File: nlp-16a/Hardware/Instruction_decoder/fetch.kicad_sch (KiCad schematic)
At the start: 50 parts

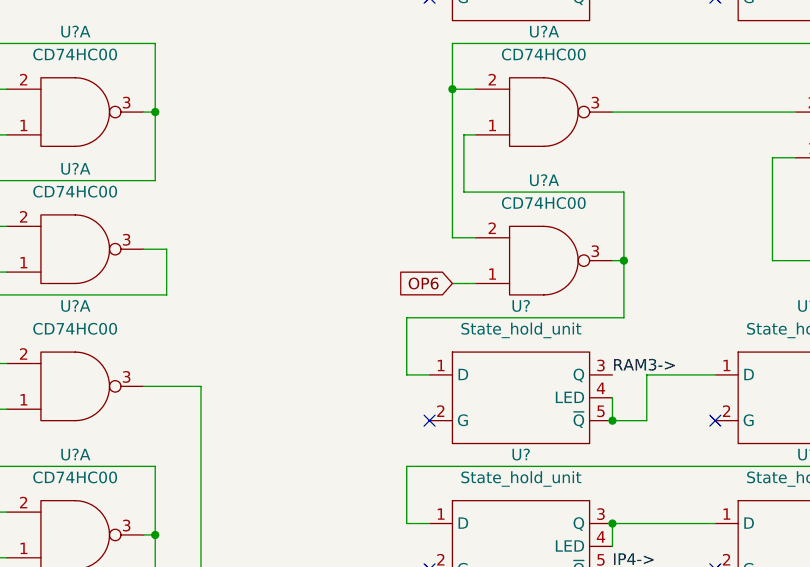
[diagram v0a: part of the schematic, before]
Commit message: 命令デコーダ 不具合修正
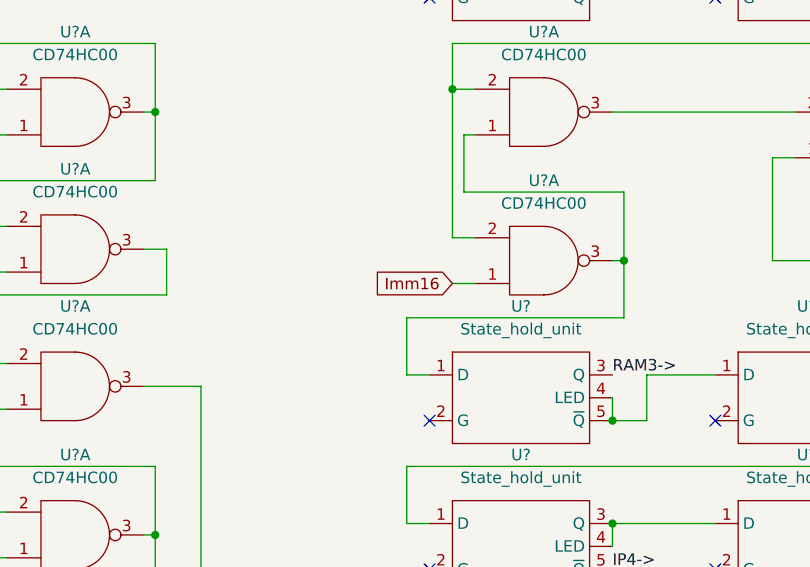
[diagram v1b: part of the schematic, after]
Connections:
- net OP6: no longer U?.1
- new net Imm16: U?.1
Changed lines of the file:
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@@
     )
   )
-  (global_label "OP6" (shape input) (at 147.32 88.9 180) (fields_autoplaced)
+  (global_label "Imm16" (shape input) (at 147.32 88.9 180) (fields_autoplaced)
     (effects (font (size 1.27 1.27)) (justify right))
-    (property "Intersheet References" "${INTERSHEET_REFS}" (id 0) (at 141.0969 88.8206 0)
+    (property "Intersheet References" "${INTERSHEET_REFS}" (id 0) (at 138.4964 88.8206 0)
       (effects (font (size 1.27 1.27)) (justify right) hide)
     )

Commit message: 命令デコーダ ロジック部の設計だいたい完了git statusgit statusやったぜ
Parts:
- removed U? (x14): CD74HC00, Package_DIP:DIP-14_W7.62mm, symbol CD74HCXX:CD74HC00
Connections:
- net ->Address1 renamed ~{->IP_SET}
- net ->Address2 renamed ~{->IP_INC1}
- net ->Address3 renamed ~{->IP_INC2}
- net ->Address4 renamed ~{->IP_INC3}
- net IP1-> renamed ~{IP_SET->}
- net IP2-> renamed ~{IP_INC1->}
- net IP3-> renamed ~{IP_INC2->}
- net IP4-> renamed ~{IP_INC3->}
- net RAM1-> renamed Fetch1->
- net RAM2-> renamed Fetch2->
- net RAM3-> renamed Fetch3->
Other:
- note added: "0 1 X X X X X X"
- note added: "1 1 0 1 X X X X"
- note added: "1 1 1 1 X X 0 X"
- note added: "1 1 1 1 X X 1 X"
- note added: "1 1 X 0 X X X X"
- note added: "Decode"
- note added: "Fetch1"
- note added: "Fetch2"
- note added: "Fetch3"
- note added: "X 0 X X X X X X"
- note removed: "-> Address"
- note removed: "INC"
- note removed: "IP ->"
- note removed: "RAM ->"
- moved on the sheet: U?, U?A

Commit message: アノテーションまで完了．基板設計に入る
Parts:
- added unit 2 of U52
- added unit 2 of U53
- gave numbers to parts that had none: 20
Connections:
- net EXE_FETCH: now also U54.6; no longer U54.3
- net GND: now also U52.4, U52.5, U52.7 (GND), U53.7 (GND)
- net OP1: now also U51.4; no longer U51.1
- net OP4: now also U50.9; no longer U50.1
- net OP5: now also U51.9; no longer U51.1
- net OP6: now also U49.12; no longer U49.1
- net OP7: now also U49.4; no longer U49.1
- net PUSH_FETCH: now also U52.8; no longer U52.3
- net VCC: now also U52.14 (VCC), U53.14 (VCC)
- net ~{EI/DI_FETCH}: now also U51.6; no longer U51.3
- net ~{POP_FETCH}: now also U50.11; no longer U50.3
- net ~{Fetch_END1}: now reaches U50.1, U50.2
- net ~{Fetch_END1}: now also U49.11, U49.9; no longer U49.1, U49.3
- net at U6.3 (Q), U6.4 (LED): now also U49.10, U49.13; no longer U49.2, U49.2
- net at U7.1 (D): now also U49.8; no longer U49.3
- net at U51.2, U52.3: now also U51.5; no longer U51.2
- net at U49.3: now also U54.4; no longer U54.1
- net at U54.3: now also U54.13; no longer U54.2
- net at U49.2, U50.3: now also U49.5; no longer U49.2
- net at U10.3 (Q), U10.4 (LED): now also U53.10, U53.13; no longer U53.2, U53.2
- net at U53.2: now also U53.8; no longer U53.3
- net at U52.1, U52.2: now also U51.12, U51.8; no longer U51.1, U51.3
- removed net Imm16: U53.1
- net ~{IR1} renamed ~{IR1_Y}
- net ~{IR2} renamed ~{IR2_Y}
- net ~{IR3} renamed ~{IR3_Y}
- new net: U11.1 (D), U53.11, U53.9
- new net: U54.10, U54.11, U54.5
- new net: U53.3, U53.4, U53.5, U54.12, U54.9
- new net: U49.1, U49.6, U50.4, U50.5
- new net: U51.10, U51.13, U52.11
- new net: U50.10, U50.13, U50.6
- new net: U50.12, U50.8, U52.12, U52.13
- new net: U51.11, U52.9
- new net: U52.10, U54.8
- new net 3word: U53.12
- new net ~{Fetch_END2}: U53.6
- no-connect marks 14 -> 15

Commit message: 基板設計 今日はとりあえずここまで
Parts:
- U1, U10, U11, U12, U13, U14, U2, U3, U4, U5, U6, U7, U8, U9: footprint (none) -> Connector_PinSocket_2.54mm:PinSocket_1x05_P2.54mm_Vertical
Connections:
- net 3word: now also U53.1; no longer U53.12
- net OP1: now also U51.1; no longer U51.4
- net OP4: now also U50.12; no longer U50.9
- net ~{->IP_INC3}: now also U53.5; no longer U53.1
- net ~{EI/DI_FETCH}: now also U51.3, U51.4; no longer U51.1, U51.6
- net ~{Fetch_END1}: now also U49.10; no longer U49.9
- net ~{Fetch_END2}: now also U53.8; no longer U53.6
- net ~{INT_FETCH}: now also U51.6; no longer U51.3
- net ~{POP_FETCH}: now also U50.8; no longer U50.11
- net at U49.13, U6.3 (Q), U6.4 (LED): now also U49.9; no longer U49.10
- net at U54.3: now also U54.12; no longer U54.13
- net at U10.3 (Q), U10.4 (LED), U53.13: now also U53.2; no longer U53.10
- net at U50.13, U50.6: now also U50.9; no longer U50.10
- net at U52.12, U52.13: now also U50.10, U50.11; no longer U50.12, U50.8
- new net: U11.1 (D), U53.12, U53.3
- new net: U53.10, U53.6, U53.9, U54.13, U54.9
- new net: U53.11, U53.4
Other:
- moved on the sheet: U50C, U50D, U51A, U51B, U53A, U53B, U53C, U53D

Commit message: 基板設計 進捗
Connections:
- net OP7: now also U49.1; no longer U49.4
- net at U54.4: now also U49.6; no longer U49.3
- net at U50.4, U50.5: now also U49.3, U49.4; no longer U49.1, U49.6
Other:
- moved on the sheet: U49A, U49B
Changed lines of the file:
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@@
     (pin "13")
   )
-  (symbol (lib_id "CD74HCXX:CD74HC00") (at 135.89 116.84 0) (mirror x) (unit 2)
-    (in_bom yes) (on_board yes)
-    (property "Reference" "U49" (id 0) (at 135.89 107.95 0))
-    (property "Value" "CD74HC00" (id 1) (at 135.89 110.49 0))
-    (property "Footprint" "Package_DIP:DIP-14_W7.62mm" (id 2) (at 135.89 123.19 0)
-      (effects (font (size 1.27 1.27)) hide)
-    )
-    (property "Datasheet" "" (id 3) (at 130.81 116.84 0))
+  (symbol (lib_id "CD74HCXX:CD74HC00") (at 135.89 100.33 0) (mirror x) (unit 2)
+    (in_bom yes) (on_board yes)
+    (property "Reference" "U49" (id 0) (at 135.89 91.44 0))
+    (property "Value" "CD74HC00" (id 1) (at 135.89 93.98 0))
+    (property "Footprint" "Package_DIP:DIP-14_W7.62mm" (id 2) (at 135.89 106.68 0)
+      (effects (font (size 1.27 1.27)) hide)
+    )
+    (property "Datasheet" "" (id 3) (at 130.81 100.33 0))
     (pin "14")
     (pin "7")
@@
     (pin "5")
   )
-  (symbol (lib_id "CD74HCXX:CD74HC00") (at 135.89 100.33 0) (mirror x) (unit 1)
-    (in_bom yes) (on_board yes)
-    (property "Reference" "U49" (id 0) (at 135.89 91.44 0))
-    (property "Value" "CD74HC00" (id 1) (at 135.89 93.98 0))
-    (property "Footprint" "Package_DIP:DIP-14_W7.62mm" (id 2) (at 135.89 106.68 0)
-      (effects (font (size 1.27 1.27)) hide)
-    )
-    (property "Datasheet" "" (id 3) (at 130.81 100.33 0))
-    (pin "14")
-    (pin "7")
+  (symbol (lib_id "CD74HCXX:CD74HC00") (at 135.89 116.84 0) (mirror x) (unit 1)
+    (in_bom yes) (on_board yes)
+    (property "Reference" "U49" (id 0) (at 135.89 107.95 0))
+    (property "Value" "CD74HC00" (id 1) (at 135.89 110.49 0))
+    (property "Footprint" "Package_DIP:DIP-14_W7.62mm" (id 2) (at 135.89 123.19 0)
+      (effects (font (size 1.27 1.27)) hide)
+    )
+    (property "Datasheet" "" (id 3) (at 130.81 116.84 0))
+    (pin "14")
+    (pin "7")
